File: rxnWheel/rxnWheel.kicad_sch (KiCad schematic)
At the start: 38 parts, among them Q10 2N3904, U1 ATmega328-P, U2 ATmega328-P, Y1 16MHz, Y2 16MHz

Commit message: changes
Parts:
- removed C10, C8, C9: 1uF, Capacitor_SMD:C_0805_2012Metric, symbol Device:C
- TP? (x3): value (none) -> Phase
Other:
- sheet U ports: added none; removed BATT+, BEMF
- sheet V ports: added none; removed BATT+, BEMF
- sheet W ports: added none; removed BATT+, BEMF
- moved on the sheet: R13, R3

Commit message: minor changes
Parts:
- removed C20, C21, C22: 1uF, Capacitor_SMD:C_0805_2012Metric, symbol Device:C
- removed R7: 100, Resistor_SMD:R_0805_2012Metric, symbol Device:R
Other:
- sheet U ports: added none; removed BRK_OUT
- sheet V ports: added none; removed BRK_OUT
- sheet W ports: added none; removed BRK_OUT

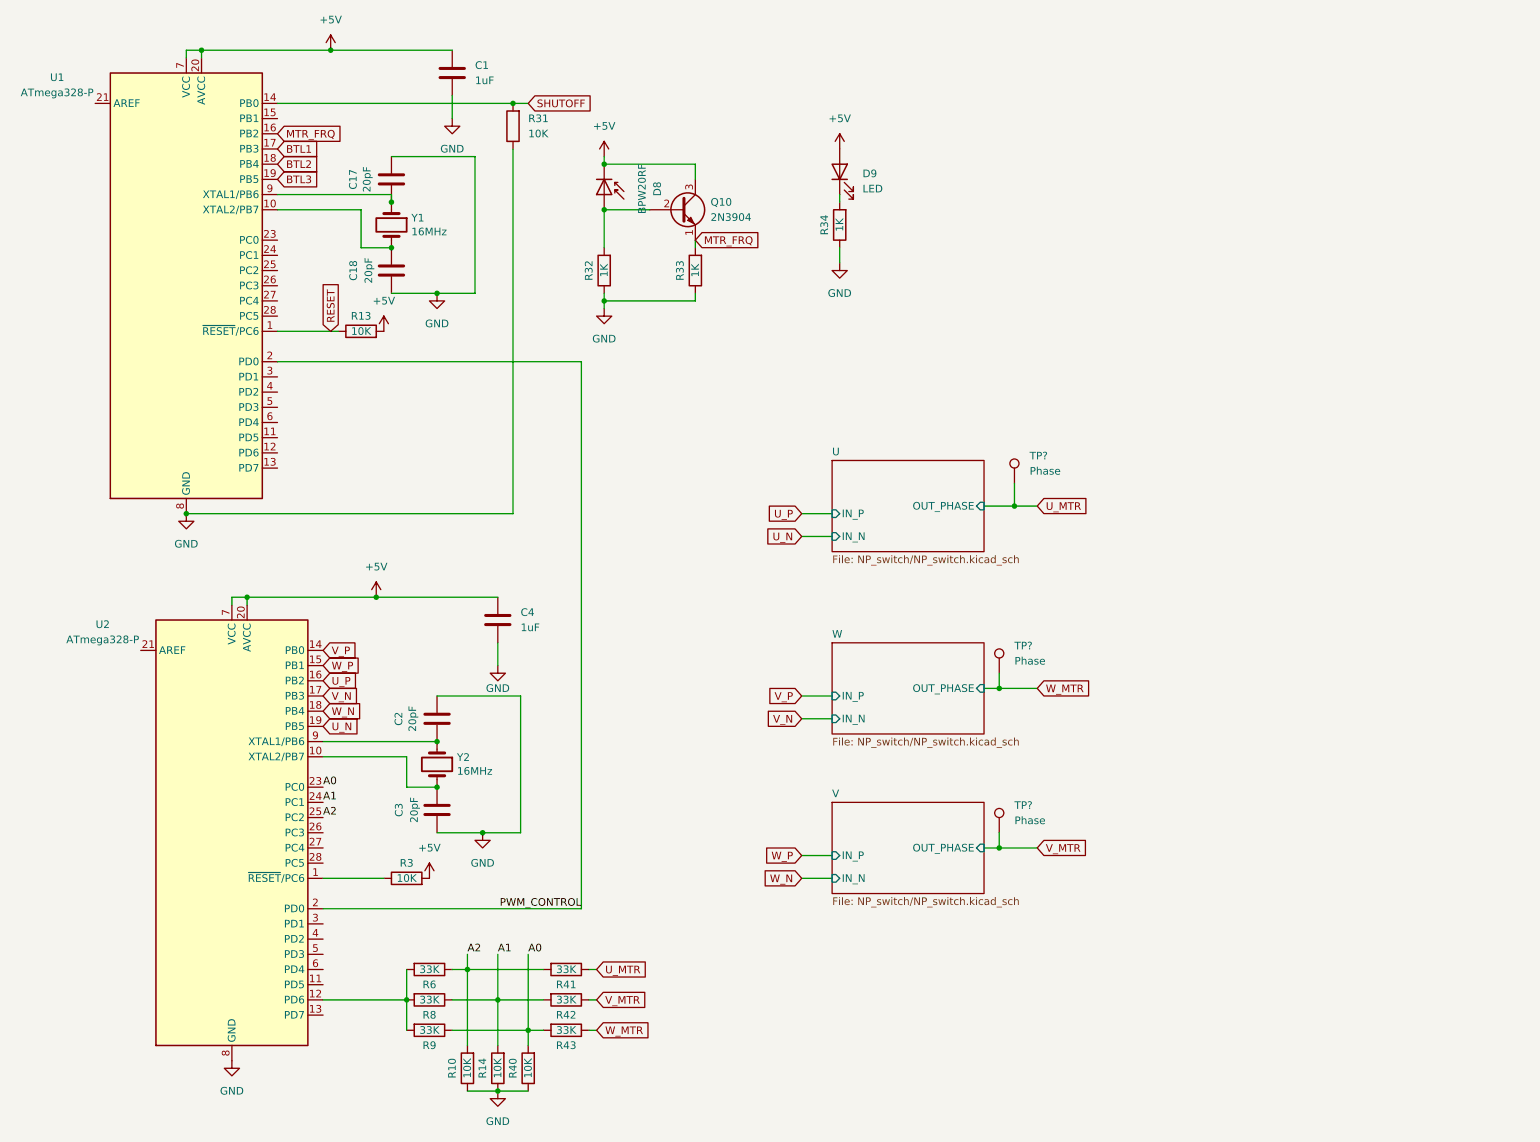
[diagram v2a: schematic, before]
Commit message: Cap
Caps vbus --> gnd
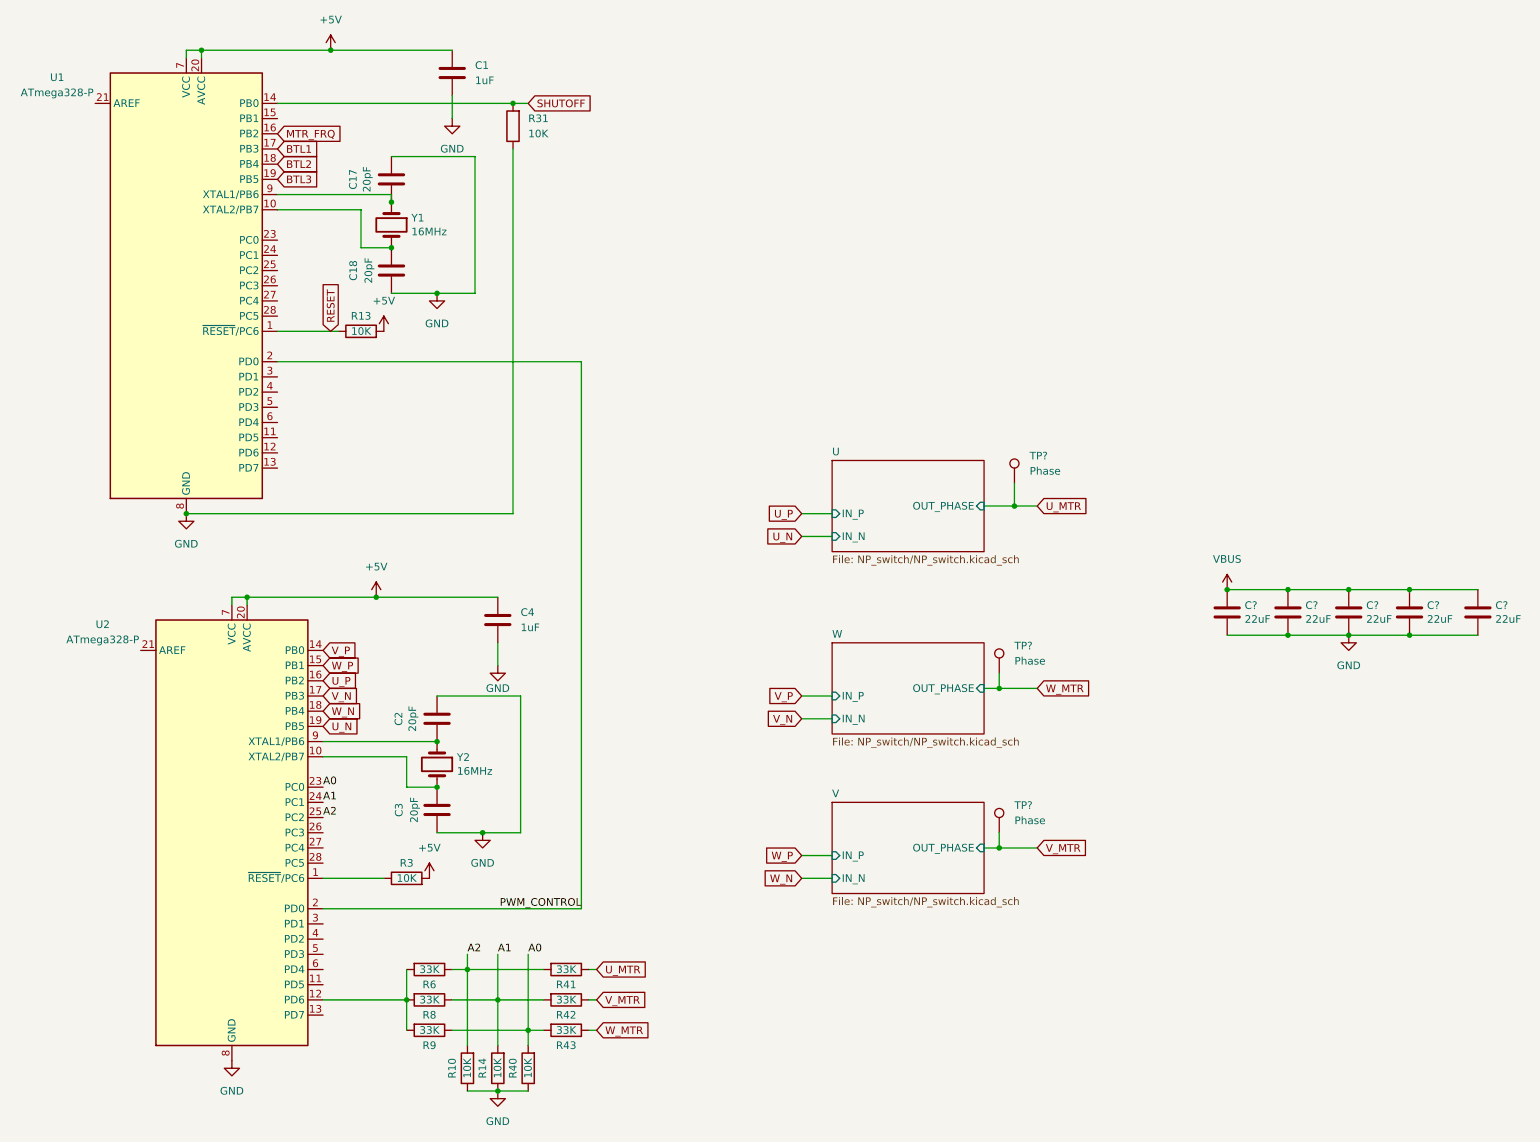
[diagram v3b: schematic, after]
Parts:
- removed D8: BPW20RF, TB9061AFNG:2x_jumper, symbol Device:D_Photo
- removed D9: LED, TB9061AFNG:2x_jumper, symbol Device:LED
- removed Q10: 2N3904, Package_TO_SOT_THT:TO-92_Inline, symbol Transistor_BJT:2N3904
- removed R32, R33, R34: 1K, Resistor_SMD:R_0805_2012Metric, symbol Device:R
- added C? (x5): 22uF, Capacitor_SMD:C_1210_3225Metric, symbol Device:C
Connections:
- net GND: now also C?.2, C?.2, C?.2, C?.2, C?.2
- new net VBUS: C?.1, C?.1, C?.1, C?.1, C?.1

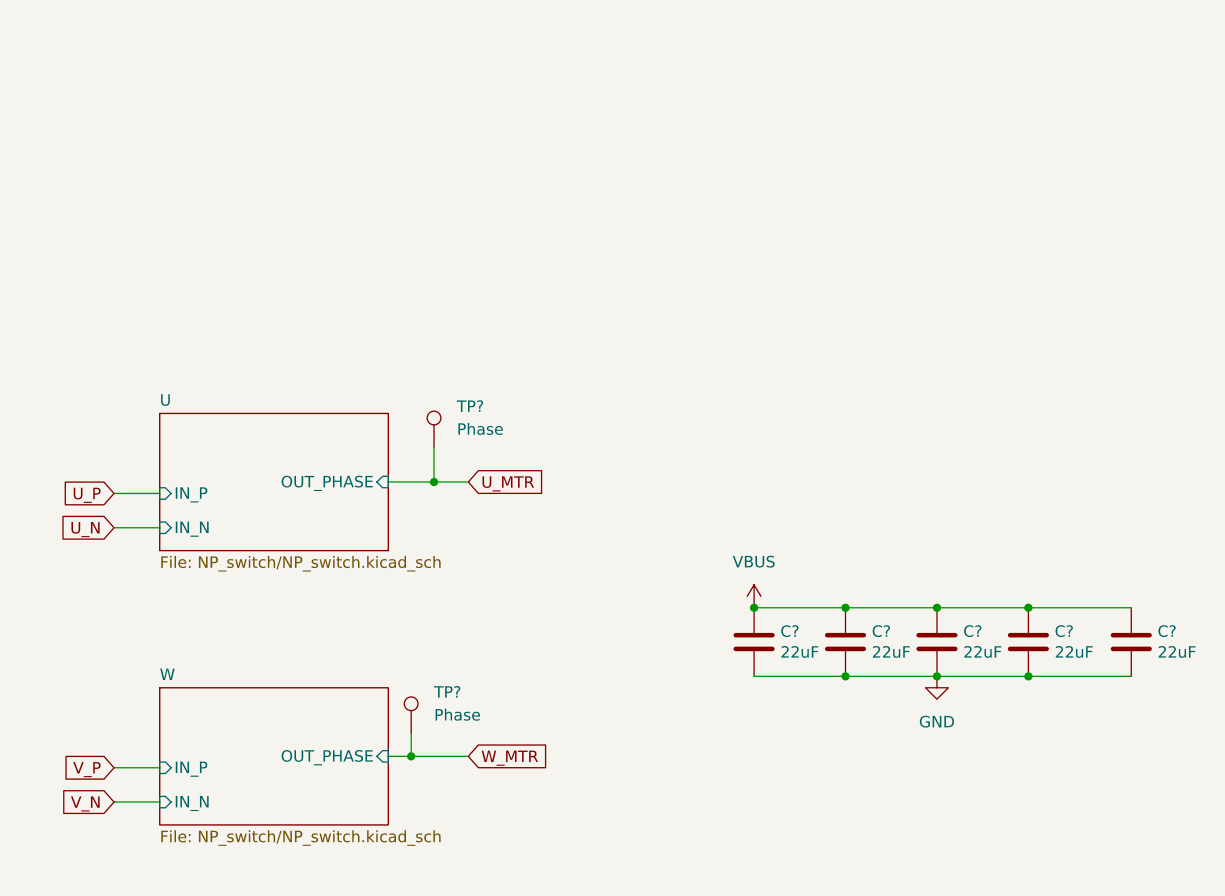
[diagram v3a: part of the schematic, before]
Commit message: corrected capacitors
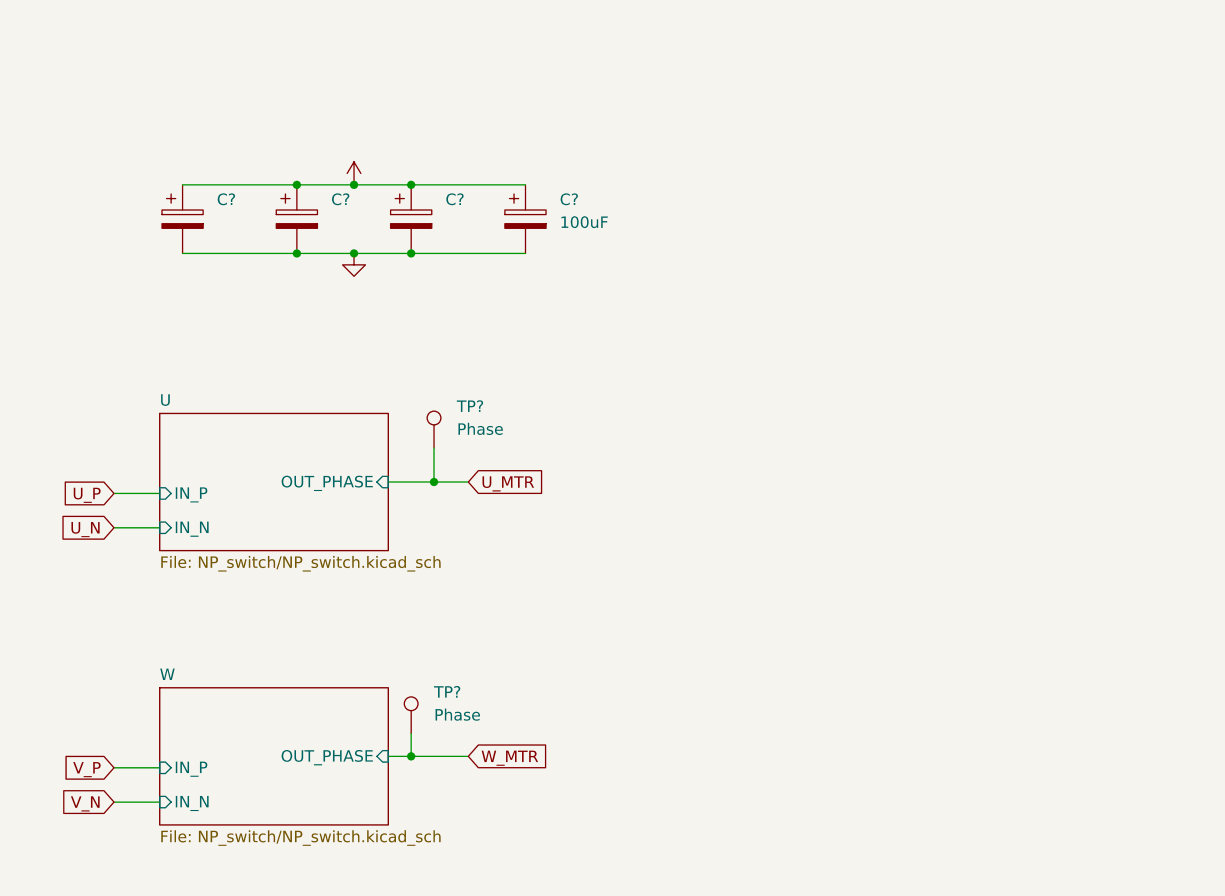
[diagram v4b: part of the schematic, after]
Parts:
- removed C? (x5): 22uF, Capacitor_SMD:C_1210_3225Metric, symbol Device:C
- added C? (x3): (no value), symbol Device:C_Polarized
- added C?: 100uF, symbol Device:C_Polarized
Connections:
- net GND: now also C?.2, C?.2, C?.2, C?.2
- net VBUS: now also C?.1, C?.1, C?.1, C?.1
